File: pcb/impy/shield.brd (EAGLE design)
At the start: 137 x 101 mm, 120 parts, among them J1 USB-2410-06, J2 SI-60062-F, J3 5V, U1 AD5933YRS, U10 LTC3406AB, U11 23LCV1024-I/SN, U13 ADG725BSU, U14 ADG725BSU, U15 ADG819BRT, U2 ADG704BRM, U3 AD8656ARZ, U4 M24C08WMN, U5 ADG706BRU, U6 DP83848I, U7 MIC2009A-1YM6, U8 AT25DF081A-SS, U9 SST25VF080B-80-4I-S2

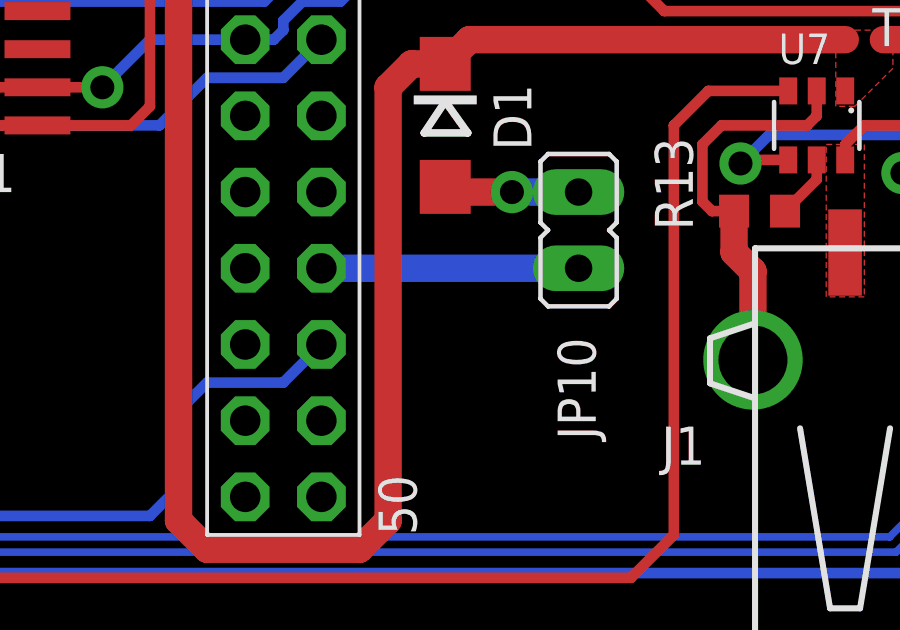
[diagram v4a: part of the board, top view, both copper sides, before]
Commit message: * pcb/impy: (shield.sch, shield.brd) Add pull down resistor to PA9 (USB device VBUS pin) to prevent the green LED from turning on while the internal pull down is not configured.
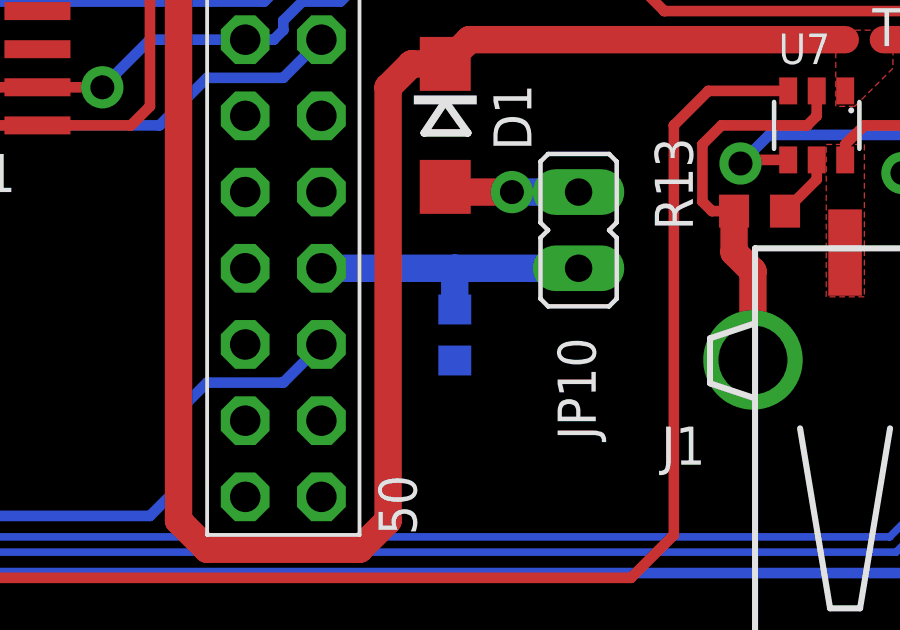
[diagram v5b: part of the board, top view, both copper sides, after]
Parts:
- added R22: 10k, rcl:R0603
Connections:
- net GND: now also R22.1
- net PA9: now also R22.2
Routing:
- net PA9: track 8.57 -> 9.94 mm
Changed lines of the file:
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@@
 <attribute name="VALUE" x="17.4625" y="40.3225" size="1.27" layer="27" rot="R90"/>
+</element>
+<element name="R22" library="rcl" package="R0603" value="10k" x="31.115" y="7.9375" smashed="yes" rot="MR90">
+<attribute name="NAME" x="31.75" y="7.3025" size="1.27" layer="26" rot="MR90"/>
+<attribute name="VALUE" x="31.75" y="7.3025" size="1.27" layer="28" rot="MR90"/>
 </element>
 </elements>
@@
 <wire x1="42.8625" y1="14.9225" x2="43.18" y2="15.24" width="0.3556" layer="1"/>
 <wire x1="43.18" y1="15.24" x2="43.18" y2="16.0725" width="0.3556" layer="1"/>
+<contactref element="R22" pad="1"/>
 </signal>
 <signal name="+5V" class="1">
@@
 <contactref element="JP2" pad="44"/>
 <contactref element="JP10" pad="1"/>
-<wire x1="35.2425" y1="10.16" x2="26.67" y2="10.16" width="0.9144" layer="16"/>
+<wire x1="35.2425" y1="10.16" x2="31.115" y2="10.16" width="0.9144" layer="16"/>
+<contactref element="R22" pad="2"/>
+<wire x1="31.115" y1="10.16" x2="26.67" y2="10.16" width="0.9144" layer="16"/>
+<wire x1="31.115" y1="8.7875" x2="31.115" y2="10.16" width="0.9144" layer="16"/>
 </signal>
 <signal name="PE2">

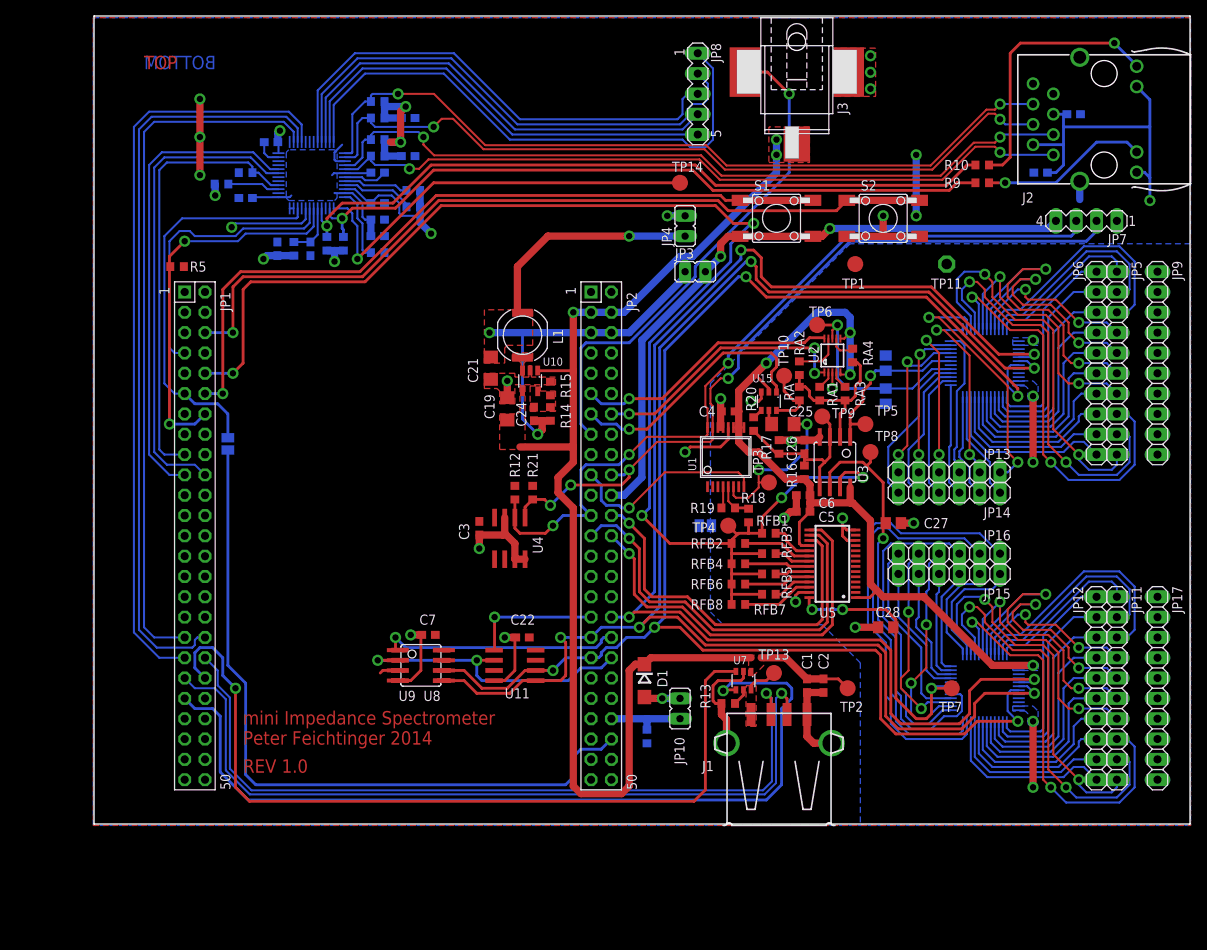
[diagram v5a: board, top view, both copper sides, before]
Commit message: * pcb/impy: (shield.brd) Add mounting holes for 3mm screws, change board size to 140x101mm and improve layout of some mux traces.
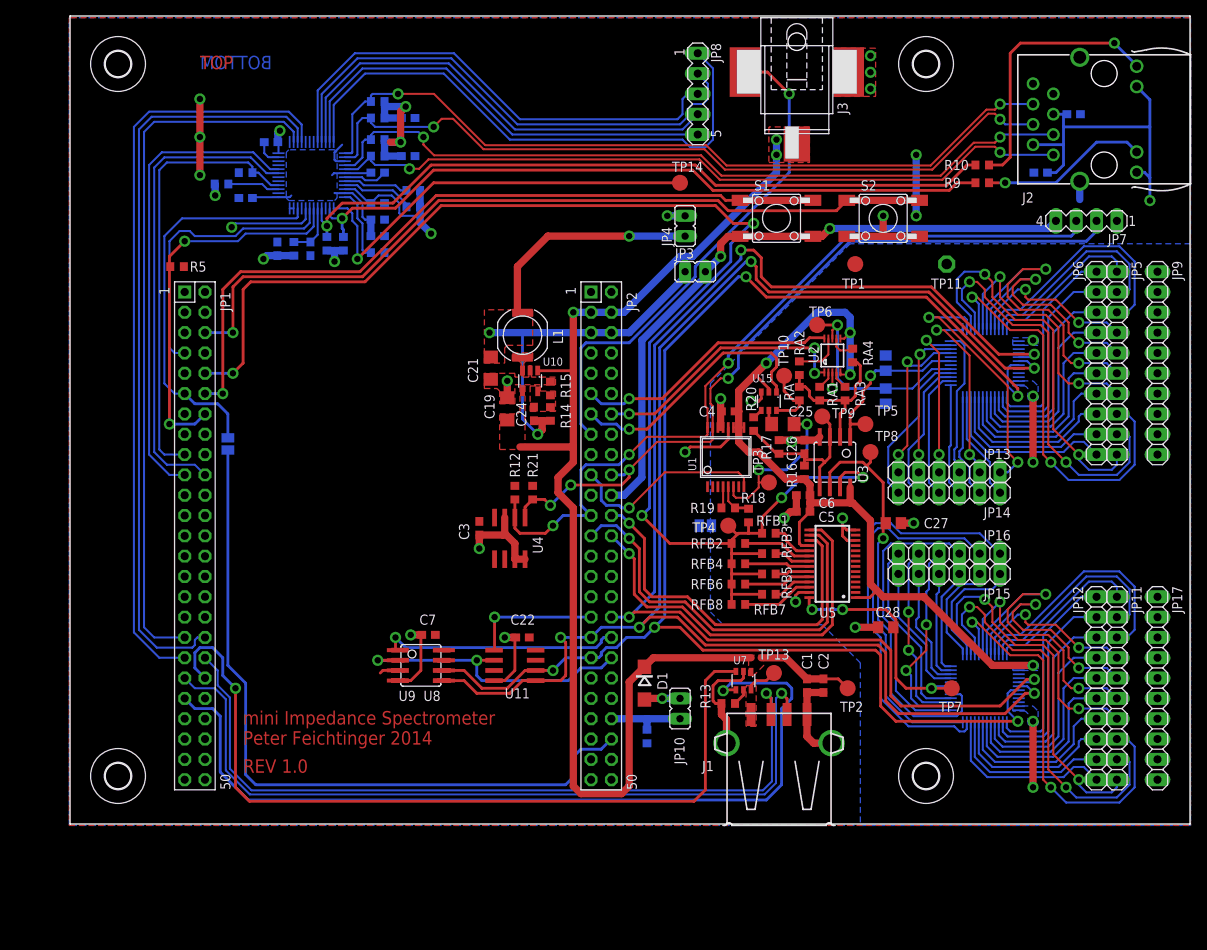
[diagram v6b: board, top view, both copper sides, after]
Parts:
- added U$1, U$2, U$3, U$4: (no value), holes:3,2
- moved D1 0.32 mm to (30.8, 14.6)
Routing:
- net N$13: track 36.8 -> 30.3 mm
- net PD2: track 166.8 -> 162.0 mm
- net PC12: track 193.9 -> 190.3 mm
- net N$97: track 49.8 -> 46.9 mm
- net N$98: track 39.0 -> 36.4 mm
- net N$12: track 55.8 -> 53.4 mm
- net N$96: track 55.8 -> 53.6 mm
- net PC10: track 188.1 -> 185.8 mm
- net N$100: track 25.4 -> 23.4 mm
- net N$99: track 27.3 -> 25.4 mm
- net +5V: track 159.2 -> 158.3 mm
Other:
- board size 137 x 101 mm -> 140 x 101 mm

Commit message: * pcb/impy: (shield.brd) Resize board to really fit a single Eurocard.
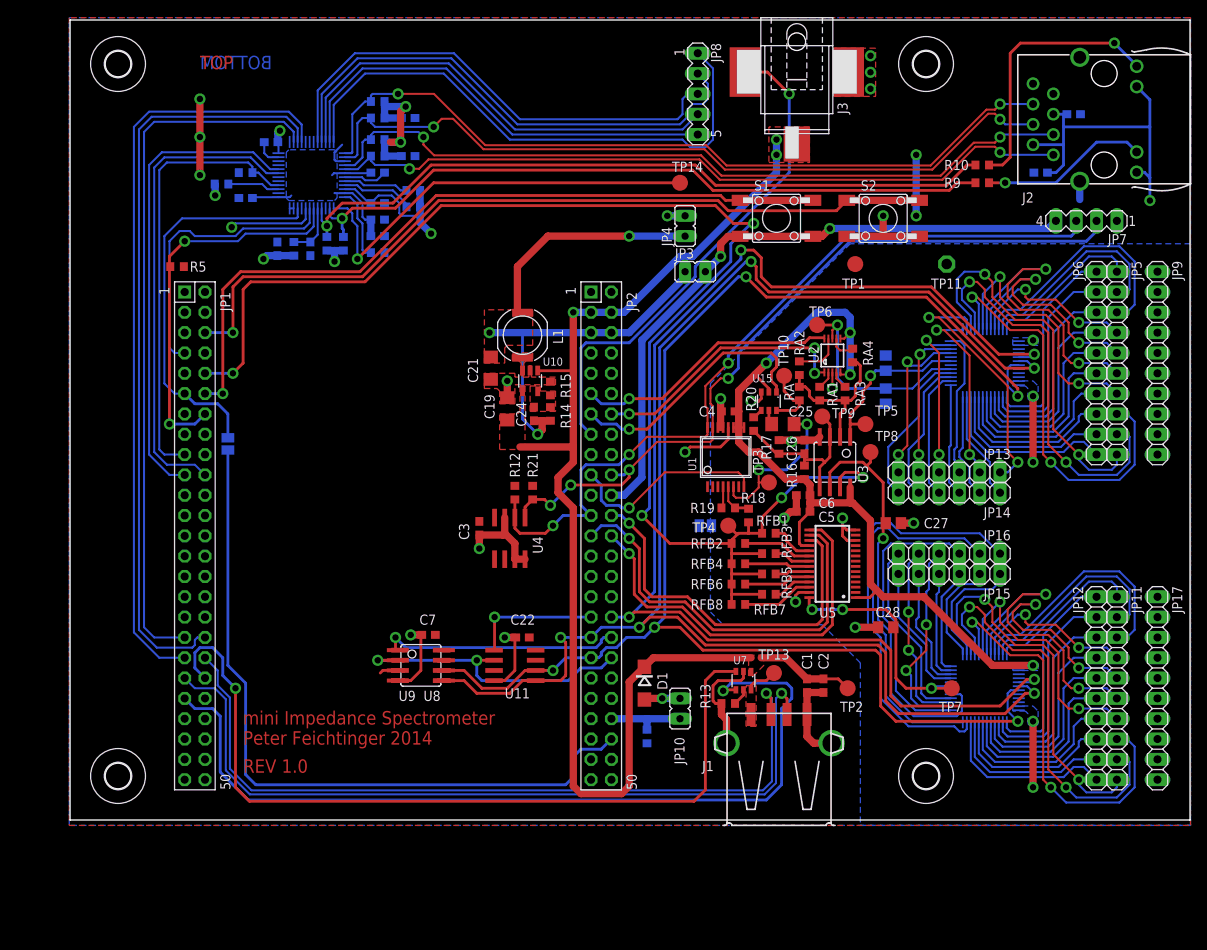
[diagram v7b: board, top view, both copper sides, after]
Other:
- board size 140 x 101 mm -> 140 x 100 mm
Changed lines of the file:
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@@
 <board>
 <plain>
-<wire x1="-41" y1="-3" x2="99" y2="-3" width="0" layer="20"/>
-<wire x1="99" y1="-3" x2="99" y2="98" width="0" layer="20"/>
-<wire x1="99" y1="98" x2="-41" y2="98" width="0" layer="20"/>
-<wire x1="-41" y1="98" x2="-41" y2="-3" width="0" layer="20"/>
+<wire x1="-41" y1="-2.5" x2="99" y2="-2.5" width="0" layer="20"/>
+<wire x1="99" y1="-2.5" x2="99" y2="97.5" width="0" layer="20"/>
+<wire x1="99" y1="97.5" x2="-41" y2="97.5" width="0" layer="20"/>
+<wire x1="-41" y1="97.5" x2="-41" y2="-2.5" width="0" layer="20"/>
 <wire x1="-33" y1="0" x2="33" y2="0" width="0.254" layer="51"/>
 <wire x1="33" y1="0" x2="33" y2="97.5" width="0.254" layer="51"/>
@@
 <wire x1="-15.225" y1="91.1225" x2="-25.0675" y2="91.1225" width="0.254" layer="42"/>
 <wire x1="-25.0675" y1="91.1225" x2="-25.0675" y2="93.345" width="0.254" layer="42"/>
-<dimension x1="-41" y1="98" x2="-41" y2="-3" x3="-46" y3="47.5" textsize="1.27" textratio="10" layer="47" width="0.1" visible="yes"/>
-<dimension x1="99" y1="98" x2="-41" y2="98" x3="29" y3="103" textsize="1.27" textratio="10" layer="47" width="0.1" visible="yes"/>
+<dimension x1="-41" y1="97.5" x2="-41" y2="-2.5" x3="-46" y3="47.5" textsize="1.27" textratio="10" layer="47" width="0.1" visible="yes"/>
+<dimension x1="99" y1="97.5" x2="-41" y2="97.5" x3="29" y3="102.5" textsize="1.27" textratio="10" layer="47" width="0.1" visible="yes"/>
 </plain>
 <attributes>

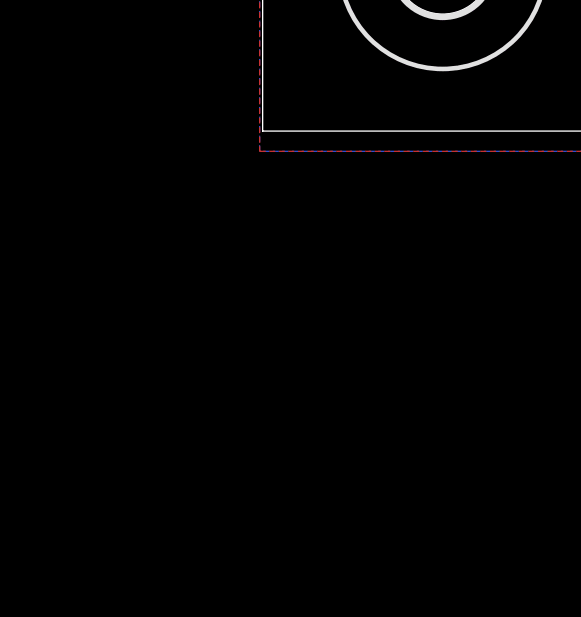
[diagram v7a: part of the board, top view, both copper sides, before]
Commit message: * pcb/impy: (shield.sch) Add various compensation capacitors to the op amps.
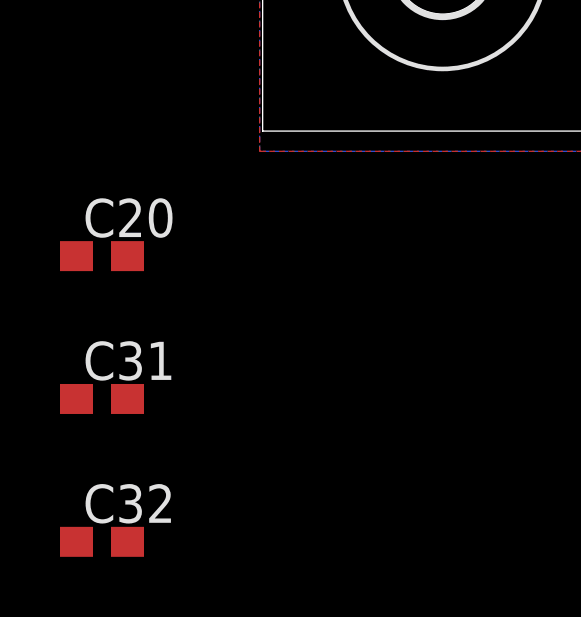
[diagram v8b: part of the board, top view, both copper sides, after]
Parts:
- added C20, C31, C32: N/A, rcl:C0603
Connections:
- net N$12: now also C31.2
- net N$14: now also C20.2
- net N$15: now also C32.2
- net N$3: now also C20.1, C32.1
- net PC2: now also C31.1
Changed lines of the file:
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@@
 <element name="U$3" library="holes" package="3,2" value="" x="66" y="92"/>
 <element name="U$4" library="holes" package="3,2" value="" x="66" y="3"/>
+<element name="C20" library="rcl" package="C0603" value="N/A" x="-46.355" y="-6.6675"/>
+<element name="C31" library="rcl" package="C0603" value="N/A" x="-46.355" y="-11.43"/>
+<element name="C32" library="rcl" package="C0603" value="N/A" x="-46.355" y="-16.1925"/>
 </elements>
 <signals>
@@
 <wire x1="56.6175" y1="49.95" x2="57.15" y2="50.4825" width="0.3556" layer="1"/>
 <wire x1="57.15" y1="50.4825" x2="57.15" y2="51.7525" width="0.3556" layer="1"/>
+<contactref element="C20" pad="1"/>
+<contactref element="C32" pad="1"/>
+<wire x1="-47.205" y1="-6.6675" x2="50.165" y2="51.65" width="0" layer="19" extent="1-1"/>
+<wire x1="-47.205" y1="-16.1925" x2="-47.205" y2="-6.6675" width="0" layer="19" extent="1-1"/>
 </signal>
 <signal name="VCC/2" class="2">
@@
 <wire x1="60.9625" y1="34.6075" x2="60.6425" y2="34.6075" width="0.3556" layer="1"/>
 <wire x1="69.85" y1="10.4775" x2="64.4525" y2="10.4775" width="0.254" layer="16"/>
+<contactref element="C31" pad="2"/>
+<wire x1="-45.505" y1="-11.43" x2="61.595" y2="13.335" width="0" layer="19" extent="1-16"/>
 </signal>
 <signal name="N$14" class="2">
@@
 <wire x1="59.055" y1="52.07" x2="59.055" y2="53.0225" width="0.3556" layer="1"/>
 <wire x1="58.42" y1="46.99" x2="56.515" y2="46.99" width="0.3556" layer="1"/>
+<contactref element="C20" pad="2"/>
+<wire x1="-45.505" y1="-6.6675" x2="56.515" y2="45.3815" width="0" layer="19" extent="1-1"/>
 </signal>
 <signal name="N$15" class="2">
@@
 <wire x1="54.2925" y1="58.7375" x2="54.9275" y2="59.3725" width="0.254" layer="1"/>
 <wire x1="54.9275" y1="59.3725" x2="52.3875" y2="59.3725" width="0.3556" layer="1"/>
+<contactref element="C32" pad="2"/>
+<wire x1="-45.505" y1="-16.1925" x2="54.9275" y2="52.705" width="0" layer="19" extent="1-16"/>
 </signal>
 <signal name="N$16" class="2">
@@
 <contactref element="RFB1" pad="2"/>
 <contactref element="U3" pad="7"/>
-<contactref element="R18" pad="2"/>
 <contactref element="RFB6" pad="2"/>
 <contactref element="RFB5" pad="2"/>
@@
 <wire x1="43.815" y1="33.3375" x2="45.505" y2="33.3375" width="0.3556" layer="1"/>
 <wire x1="41.695" y1="25.7175" x2="41.695" y2="24.4475" width="0.3556" layer="1"/>
-<wire x1="43.815" y1="34.71" x2="43.815" y2="33.3375" width="0.3556" layer="1"/>
 <wire x1="43.815" y1="33.3375" x2="42.545" y2="33.3375" width="0.3556" layer="1"/>
 <wire x1="42.545" y1="33.3375" x2="42.38625" y2="33.17875" width="0.3556" layer="1"/>
@@
 <wire x1="39.6875" y1="74.295" x2="41.91" y2="72.0725" width="0.3556" layer="1"/>
 <wire x1="41.91" y1="72.0725" x2="44.45" y2="72.0725" width="0.3556" layer="1"/>
+<contactref element="R18" pad="2"/>
+<wire x1="43.815" y1="34.71" x2="43.815" y2="33.3375" width="0.3556" layer="1"/>
+<contactref element="C31" pad="1"/>
+<wire x1="-24.13" y1="53.34" x2="-47.205" y2="-11.43" width="0" layer="19" extent="1-1"/>
 </signal>
 <signal name="N$2">
